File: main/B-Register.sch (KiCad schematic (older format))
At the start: 19 parts, among them U83 74LS245, U84 74LS173, U85 74LS173

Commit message: Replot main with symbols
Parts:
- renumbered D78 to D70, D79 to D71, D80 to D72, D81 to D73, D82 to D74, D83 to D75, D84 to D76, D85 to D77, R84 to R76, R85 to R77, R86 to R78, R87 to R79, R88 to R80, R89 to R81, R90 to R82, R91 to R83, U83 to U68, U84 to U69, U85 to U70
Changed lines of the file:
@@
 Sheet 19 26
 Title "B Register"
-Date "2019-11-13"
+Date "2019-11-17"
 Rev "v1.0"
 Comp "Christopher Milan"
@@
 AR Path="/5D9C722C/5D9D1D45" Ref="U?"  Part="1"
 AR Path="/5D9C73BD/5D9D1D45" Ref="U?"  Part="1"
-AR Path="/5DA98D6D/5DA9A5B3/5D9D1D45" Ref="U83"  Part="1"
+AR Path="/5DA98D6D/5DA9A5B3/5D9D1D45" Ref="U68"  Part="1"
 AR Path="/5DA9B7A7/5D9D1D45" Ref="U?"  Part="1"
-F 0 "U83" V 3346 1906 50  0000 R CNN
+F 0 "U68" V 3346 1906 50  0000 R CNN
 F 1 "74LS245" V 3255 1906 50  0000 R CNN
 F 2 "" H 3300 2750 50  0001 C CNN
@@
 AR Path="/5D9C722C/5D9D1D72" Ref="U?"  Part="1"
 AR Path="/5D9C73BD/5D9D1D72" Ref="U?"  Part="1"
-AR Path="/5DA98D6D/5DA9A5B3/5D9D1D72" Ref="U85"  Part="1"
+AR Path="/5DA98D6D/5DA9A5B3/5D9D1D72" Ref="U70"  Part="1"
 AR Path="/5DA9B7A7/5D9D1D72" Ref="U?"  Part="1"
-F 0 "U85" V 7854 3694 50  0000 L CNN
+F 0 "U70" V 7854 3694 50  0000 L CNN
 F 1 "74LS173" V 7945 3694 50  0000 L CNN
 F 2 "" H 7900 2750 50  0001 C CNN
@@
 AR Path="/5D9C722C/5D9D1D9C" Ref="D?"  Part="1"
 AR Path="/5D9C73BD/5D9D1D9C" Ref="D?"  Part="1"
-AR Path="/5DA98D6D/5DA9A5B3/5D9D1D9C" Ref="D78"  Part="1"
+AR Path="/5DA98D6D/5DA9A5B3/5D9D1D9C" Ref="D70"  Part="1"
 AR Path="/5DA9B7A7/5D9D1D9C" Ref="D?"  Part="1"
-F 0 "D78" V 3889 5133 50  0000 R CNN
+F 0 "D70" V 3889 5133 50  0000 R CNN
 F 1 "LED" V 3798 5133 50  0000 R CNN
 F 2 "" H 3850 5250 50  0001 C CNN
@@
 AR Path="/5D9C722C/5D9D1DA2" Ref="D?"  Part="1"
 AR Path="/5D9C73BD/5D9D1DA2" Ref="D?"  Part="1"
-AR Path="/5DA98D6D/5DA9A5B3/5D9D1DA2" Ref="D79"  Part="1"
+AR Path="/5DA98D6D/5DA9A5B3/5D9D1DA2" Ref="D71"  Part="1"
 AR Path="/5DA9B7A7/5D9D1DA2" Ref="D?"  Part="1"
-F 0 "D79" V 4239 5133 50  0000 R CNN
+F 0 "D71" V 4239 5133 50  0000 R CNN
 F 1 "LED" V 4148 5133 50  0000 R CNN
 F 2 "" H 4200 5250 50  0001 C CNN
@@
 AR Path="/5D9C722C/5D9D1DA8" Ref="D?"  Part="1"
 AR Path="/5D9C73BD/5D9D1DA8" Ref="D?"  Part="1"
-AR Path="/5DA98D6D/5DA9A5B3/5D9D1DA8" Ref="D80"  Part="1"
+AR Path="/5DA98D6D/5DA9A5B3/5D9D1DA8" Ref="D72"  Part="1"
 AR Path="/5DA9B7A7/5D9D1DA8" Ref="D?"  Part="1"
-F 0 "D80" V 4589 5133 50  0000 R CNN
+F 0 "D72" V 4589 5133 50  0000 R CNN
 F 1 "LED" V 4498 5133 50  0000 R CNN
 F 2 "" H 4550 5250 50  0001 C CNN
@@
 AR Path="/5D9C722C/5D9D1DAE" Ref="D?"  Part="1"
 AR Path="/5D9C73BD/5D9D1DAE" Ref="D?"  Part="1"
-AR Path="/5DA98D6D/5DA9A5B3/5D9D1DAE" Ref="D81"  Part="1"
+AR Path="/5DA98D6D/5DA9A5B3/5D9D1DAE" Ref="D73"  Part="1"
 AR Path="/5DA9B7A7/5D9D1DAE" Ref="D?"  Part="1"
-F 0 "D81" V 4939 5133 50  0000 R CNN
+F 0 "D73" V 4939 5133 50  0000 R CNN
 F 1 "LED" V 4848 5133 50  0000 R CNN
 F 2 "" H 4900 5250 50  0001 C CNN
@@
 AR Path="/5D9C722C/5D9D1DB4" Ref="D?"  Part="1"
 AR Path="/5D9C73BD/5D9D1DB4" Ref="D?"  Part="1"
-AR Path="/5DA98D6D/5DA9A5B3/5D9D1DB4" Ref="D82"  Part="1"
+AR Path="/5DA98D6D/5DA9A5B3/5D9D1DB4" Ref="D74"  Part="1"
 AR Path="/5DA9B7A7/5D9D1DB4" Ref="D?"  Part="1"
-F 0 "D82" V 5289 5133 50  0000 R CNN
+F 0 "D74" V 5289 5133 50  0000 R CNN
 F 1 "LED" V 5198 5133 50  0000 R CNN
 F 2 "" H 5250 5250 50  0001 C CNN
@@
 AR Path="/5D9C722C/5D9D1DBA" Ref="D?"  Part="1"
 AR Path="/5D9C73BD/5D9D1DBA" Ref="D?"  Part="1"
-AR Path="/5DA98D6D/5DA9A5B3/5D9D1DBA" Ref="D83"  Part="1"
+AR Path="/5DA98D6D/5DA9A5B3/5D9D1DBA" Ref="D75"  Part="1"
 AR Path="/5DA9B7A7/5D9D1DBA" Ref="D?"  Part="1"
-F 0 "D83" V 5639 5133 50  0000 R CNN
+F 0 "D75" V 5639 5133 50  0000 R CNN
 F 1 "LED" V 5548 5133 50  0000 R CNN
 F 2 "" H 5600 5250 50  0001 C CNN
@@
 AR Path="/5D9C722C/5D9D1DC0" Ref="D?"  Part="1"
 AR Path="/5D9C73BD/5D9D1DC0" Ref="D?"  Part="1"
-AR Path="/5DA98D6D/5DA9A5B3/5D9D1DC0" Ref="D84"  Part="1"
+AR Path="/5DA98D6D/5DA9A5B3/5D9D1DC0" Ref="D76"  Part="1"
 AR Path="/5DA9B7A7/5D9D1DC0" Ref="D?"  Part="1"
-F 0 "D84" V 5989 5133 50  0000 R CNN
+F 0 "D76" V 5989 5133 50  0000 R CNN
 F 1 "LED" V 5898 5133 50  0000 R CNN
 F 2 "" H 5950 5250 50  0001 C CNN
@@
 AR Path="/5D9C722C/5D9D1DC6" Ref="D?"  Part="1"
 AR Path="/5D9C73BD/5D9D1DC6" Ref="D?"  Part="1"
-AR Path="/5DA98D6D/5DA9A5B3/5D9D1DC6" Ref="D85"  Part="1"
+AR Path="/5DA98D6D/5DA9A5B3/5D9D1DC6" Ref="D77"  Part="1"
 AR Path="/5DA9B7A7/5D9D1DC6" Ref="D?"  Part="1"
-F 0 "D85" V 6339 5133 50  0000 R CNN
+F 0 "D77" V 6339 5133 50  0000 R CNN
 F 1 "LED" V 6248 5133 50  0000 R CNN
 F 2 "" H 6300 5250 50  0001 C CNN
@@
 AR Path="/5D9C722C/5D9D1DE2" Ref="R?"  Part="1"
 AR Path="/5D9C73BD/5D9D1DE2" Ref="R?"  Part="1"
-AR Path="/5DA98D6D/5DA9A5B3/5D9D1DE2" Ref="R84"  Part="1"
+AR Path="/5DA98D6D/5DA9A5B3/5D9D1DE2" Ref="R76"  Part="1"
 AR Path="/5DA9B7A7/5D9D1DE2" Ref="R?"  Part="1"
-F 0 "R84" H 3920 5846 50  0000 L CNN
+F 0 "R76" H 3920 5846 50  0000 L CNN
 F 1 "220" H 3920 5755 50  0000 L CNN
 F 2 "" V 3780 5800 50  0001 C CNN
@@
 AR Path="/5D9C722C/5D9D1DE8" Ref="R?"  Part="1"
 AR Path="/5D9C73BD/5D9D1DE8" Ref="R?"  Part="1"
-AR Path="/5DA98D6D/5DA9A5B3/5D9D1DE8" Ref="R85"  Part="1"
+AR Path="/5DA98D6D/5DA9A5B3/5D9D1DE8" Ref="R77"  Part="1"
 AR Path="/5DA9B7A7/5D9D1DE8" Ref="R?"  Part="1"
-F 0 "R85" H 4270 5846 50  0000 L CNN
+F 0 "R77" H 4270 5846 50  0000 L CNN
 F 1 "220" H 4270 5755 50  0000 L CNN
 F 2 "" V 4130 5800 50  0001 C CNN
@@
 AR Path="/5D9C722C/5D9D1DEE" Ref="R?"  Part="1"
 AR Path="/5D9C73BD/5D9D1DEE" Ref="R?"  Part="1"
-AR Path="/5DA98D6D/5DA9A5B3/5D9D1DEE" Ref="R86"  Part="1"
+AR Path="/5DA98D6D/5DA9A5B3/5D9D1DEE" Ref="R78"  Part="1"
 AR Path="/5DA9B7A7/5D9D1DEE" Ref="R?"  Part="1"
-F 0 "R86" H 4620 5846 50  0000 L CNN
+F 0 "R78" H 4620 5846 50  0000 L CNN
 F 1 "220" H 4620 5755 50  0000 L CNN
 F 2 "" V 4480 5800 50  0001 C CNN
@@
 AR Path="/5D9C722C/5D9D1DF4" Ref="R?"  Part="1"
 AR Path="/5D9C73BD/5D9D1DF4" Ref="R?"  Part="1"
-AR Path="/5DA98D6D/5DA9A5B3/5D9D1DF4" Ref="R87"  Part="1"
+AR Path="/5DA98D6D/5DA9A5B3/5D9D1DF4" Ref="R79"  Part="1"
 AR Path="/5DA9B7A7/5D9D1DF4" Ref="R?"  Part="1"
-F 0 "R87" H 4970 5846 50  0000 L CNN
+F 0 "R79" H 4970 5846 50  0000 L CNN
 F 1 "220" H 4970 5755 50  0000 L CNN
 F 2 "" V 4830 5800 50  0001 C CNN
@@
 AR Path="/5D9C722C/5D9D1DFA" Ref="R?"  Part="1"
 AR Path="/5D9C73BD/5D9D1DFA" Ref="R?"  Part="1"
-AR Path="/5DA98D6D/5DA9A5B3/5D9D1DFA" Ref="R88"  Part="1"
+AR Path="/5DA98D6D/5DA9A5B3/5D9D1DFA" Ref="R80"  Part="1"
 AR Path="/5DA9B7A7/5D9D1DFA" Ref="R?"  Part="1"
-F 0 "R88" H 5320 5846 50  0000 L CNN
+F 0 "R80" H 5320 5846 50  0000 L CNN
 F 1 "220" H 5320 5755 50  0000 L CNN
 F 2 "" V 5180 5800 50  0001 C CNN
@@
 AR Path="/5D9C722C/5D9D1E00" Ref="R?"  Part="1"
 AR Path="/5D9C73BD/5D9D1E00" Ref="R?"  Part="1"
-AR Path="/5DA98D6D/5DA9A5B3/5D9D1E00" Ref="R89"  Part="1"
+AR Path="/5DA98D6D/5DA9A5B3/5D9D1E00" Ref="R81"  Part="1"
 AR Path="/5DA9B7A7/5D9D1E00" Ref="R?"  Part="1"
-F 0 "R89" H 5670 5846 50  0000 L CNN
+F 0 "R81" H 5670 5846 50  0000 L CNN
 F 1 "220" H 5670 5755 50  0000 L CNN
 F 2 "" V 5530 5800 50  0001 C CNN
@@
 AR Path="/5D9C722C/5D9D1E06" Ref="R?"  Part="1"
 AR Path="/5D9C73BD/5D9D1E06" Ref="R?"  Part="1"
-AR Path="/5DA98D6D/5DA9A5B3/5D9D1E06" Ref="R90"  Part="1"
+AR Path="/5DA98D6D/5DA9A5B3/5D9D1E06" Ref="R82"  Part="1"
 AR Path="/5DA9B7A7/5D9D1E06" Ref="R?"  Part="1"
-F 0 "R90" H 6020 5846 50  0000 L CNN
+F 0 "R82" H 6020 5846 50  0000 L CNN
 F 1 "220" H 6020 5755 50  0000 L CNN
 F 2 "" V 5880 5800 50  0001 C CNN
@@
 AR Path="/5D9C722C/5D9D1E0C" Ref="R?"  Part="1"
 AR Path="/5D9C73BD/5D9D1E0C" Ref="R?"  Part="1"
-AR Path="/5DA98D6D/5DA9A5B3/5D9D1E0C" Ref="R91"  Part="1"
+AR Path="/5DA98D6D/5DA9A5B3/5D9D1E0C" Ref="R83"  Part="1"
 AR Path="/5DA9B7A7/5D9D1E0C" Ref="R?"  Part="1"
-F 0 "R91" H 6370 5846 50  0000 L CNN
+F 0 "R83" H 6370 5846 50  0000 L CNN
 F 1 "220" H 6370 5755 50  0000 L CNN
 F 2 "" V 6230 5800 50  0001 C CNN
@@
 AR Path="/5D9C722C/5D9D1E5D" Ref="U?"  Part="1"
 AR Path="/5D9C73BD/5D9D1E5D" Ref="U?"  Part="1"
-AR Path="/5DA98D6D/5DA9A5B3/5D9D1E5D" Ref="U84"  Part="1"
+AR Path="/5DA98D6D/5DA9A5B3/5D9D1E5D" Ref="U69"  Part="1"
 AR Path="/5DA9B7A7/5D9D1E5D" Ref="U?"  Part="1"
-F 0 "U84" V 5604 3694 50  0000 L CNN
+F 0 "U69" V 5604 3694 50  0000 L CNN
 F 1 "74LS173" V 5695 3694 50  0000 L CNN
 F 2 "" H 5650 2750 50  0001 C CNN

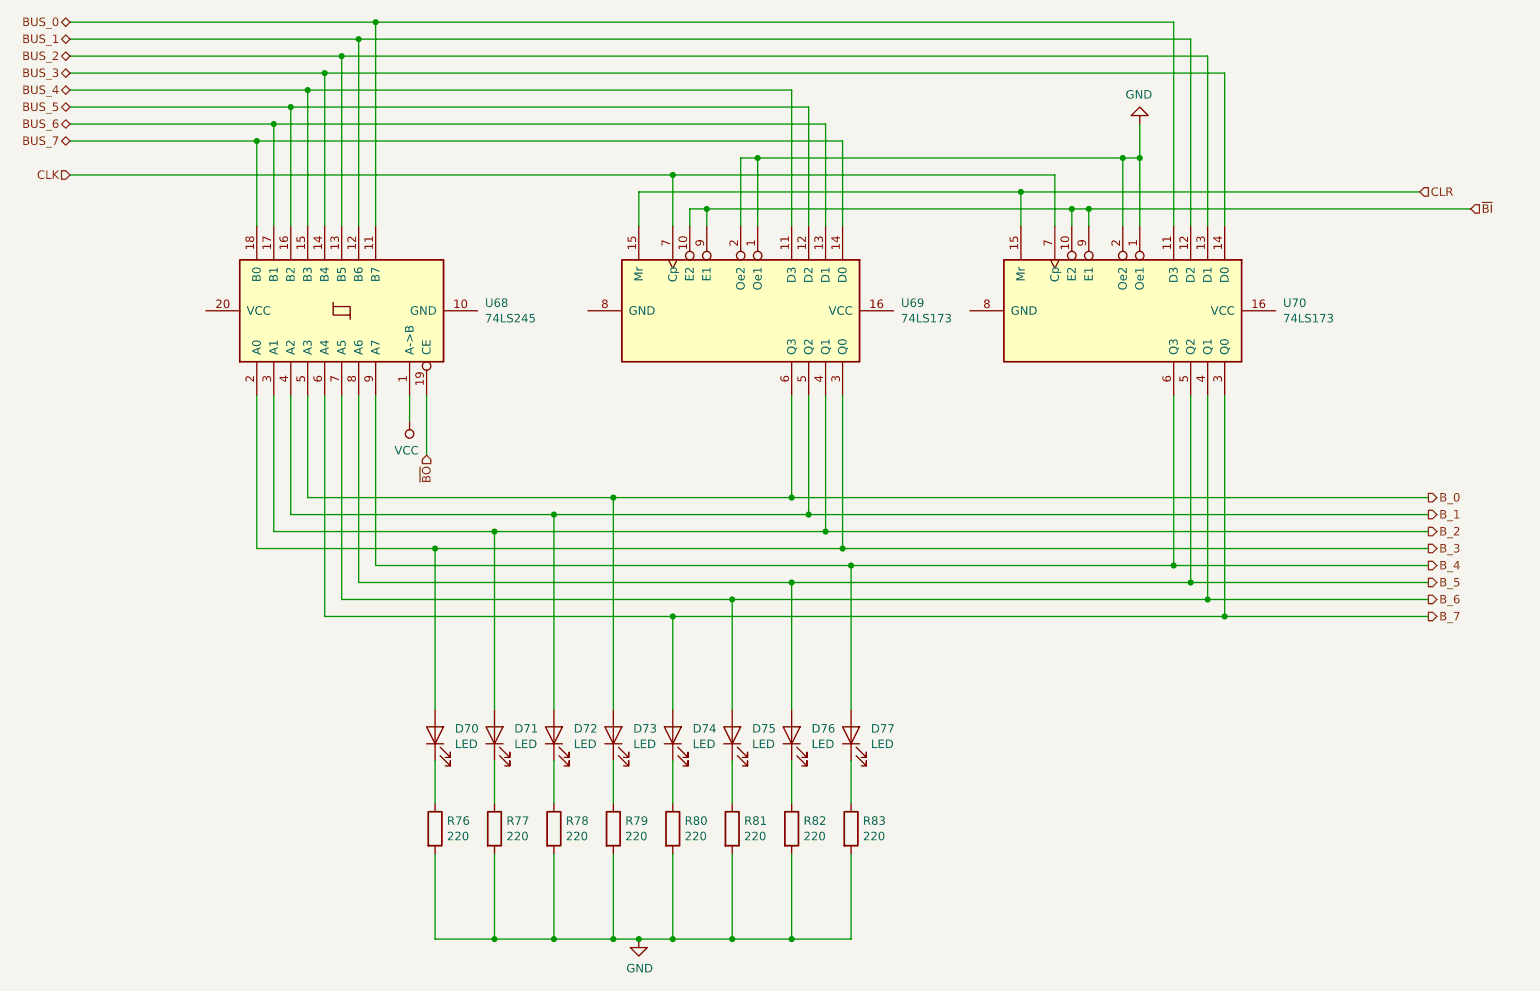
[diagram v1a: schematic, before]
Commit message: Switch to using 74LS377 in place of two 74LS173
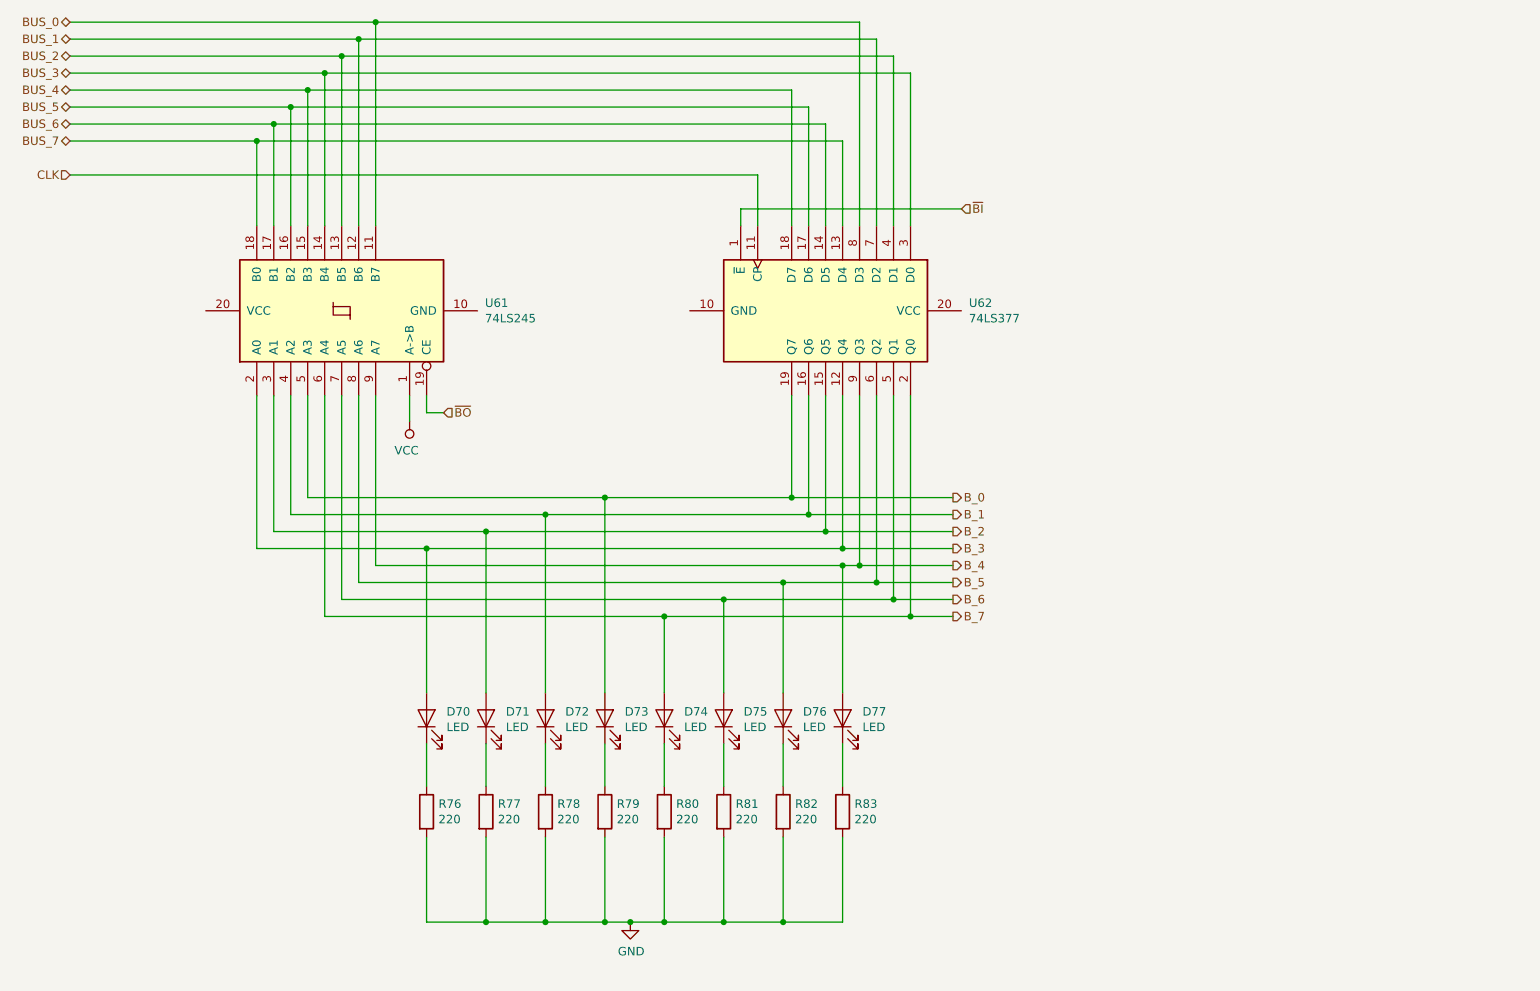
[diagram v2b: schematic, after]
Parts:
- removed U68: 74LS245, symbol 74xx:74LS245
- removed U69, U70: 74LS173, symbol 74xx:74LS173
- added U61: 74LS245, symbol 74xx:74LS245
- added U62: 74LS377, symbol 74xx:74LS377
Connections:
- net BUS_0: now also U61.11 (B7), U62.8 (D3)
- net BUS_1: now also U61.12 (B6), U62.7 (D2)
- net BUS_2: now also U61.13 (B5), U62.4 (D1)
- net BUS_3: now also U61.14 (B4), U62.3 (D0)
- net BUS_4: now also U61.15 (B3), U62.18 (D7)
- net BUS_5: now also U61.16 (B2), U62.17 (D6)
- net BUS_6: now also U61.17 (B1), U62.14 (D5)
- net BUS_7: now also U61.18 (B0), U62.13 (D4)
- net B_0: now also U61.5 (A3), U62.19 (Q7)
- net B_1: now also U61.4 (A2), U62.16 (Q6)
- net B_2: now also U61.3 (A1), U62.15 (Q5)
- net B_3: now also U61.2 (A0), U62.12 (Q4)
- net B_4: now also U61.9 (A7), U62.9 (Q3)
- net B_5: now also U61.8 (A6), U62.6 (Q2)
- net B_6: now also U61.7 (A5), U62.5 (Q1)
- net B_7: now also U61.6 (A4), U62.2 (Q0)
- net CLK: now also U62.11 (CP)
- net VCC: now also U61.1 (A->B)
- net ~BI~: now also U62.1 (~E)
- net ~BO~: now also U61.19 (CE)
